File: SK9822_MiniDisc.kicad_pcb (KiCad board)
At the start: 4 copper layers, 220 x 220 mm, 342 parts, among them P1 CONN_01X04, P2 CONN_01X04

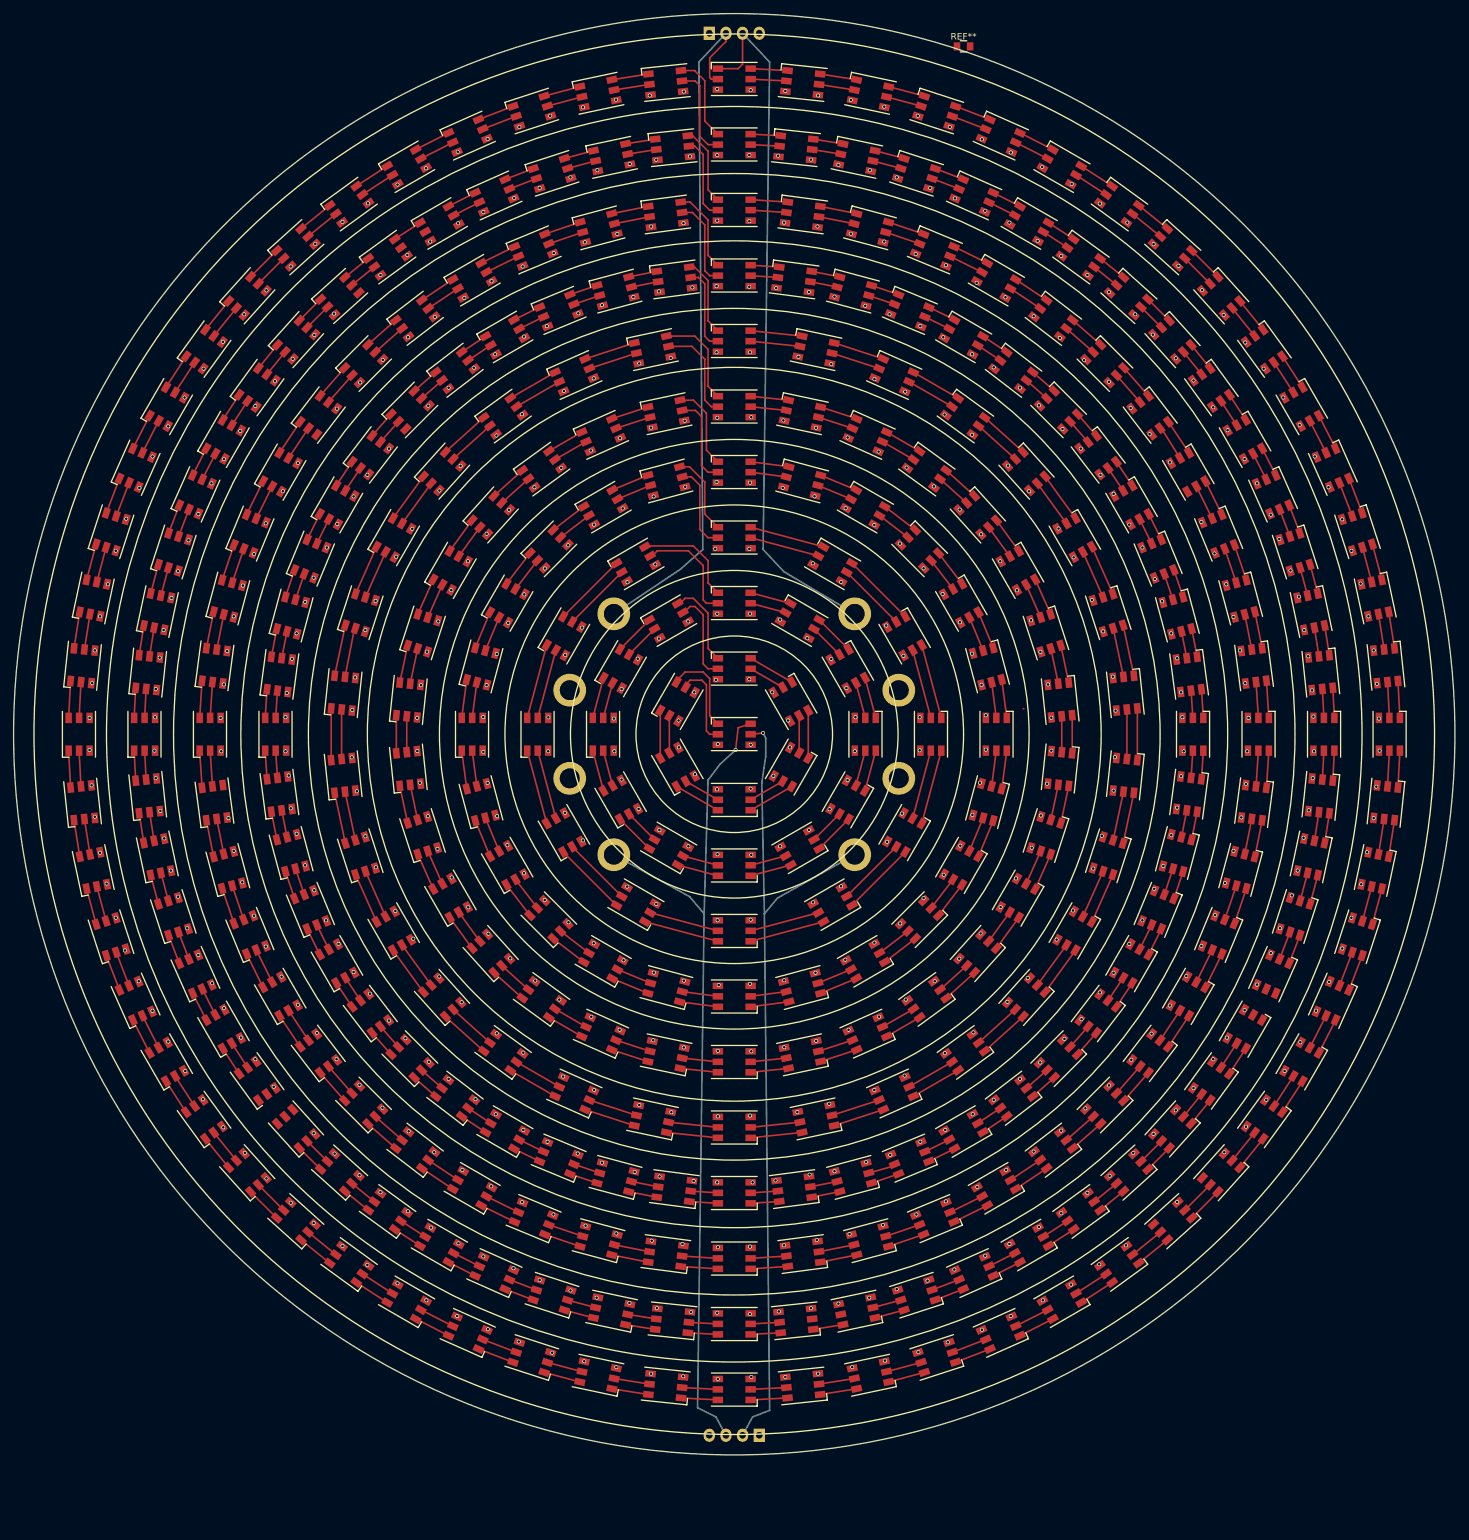
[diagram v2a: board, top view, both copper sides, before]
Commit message: places caps
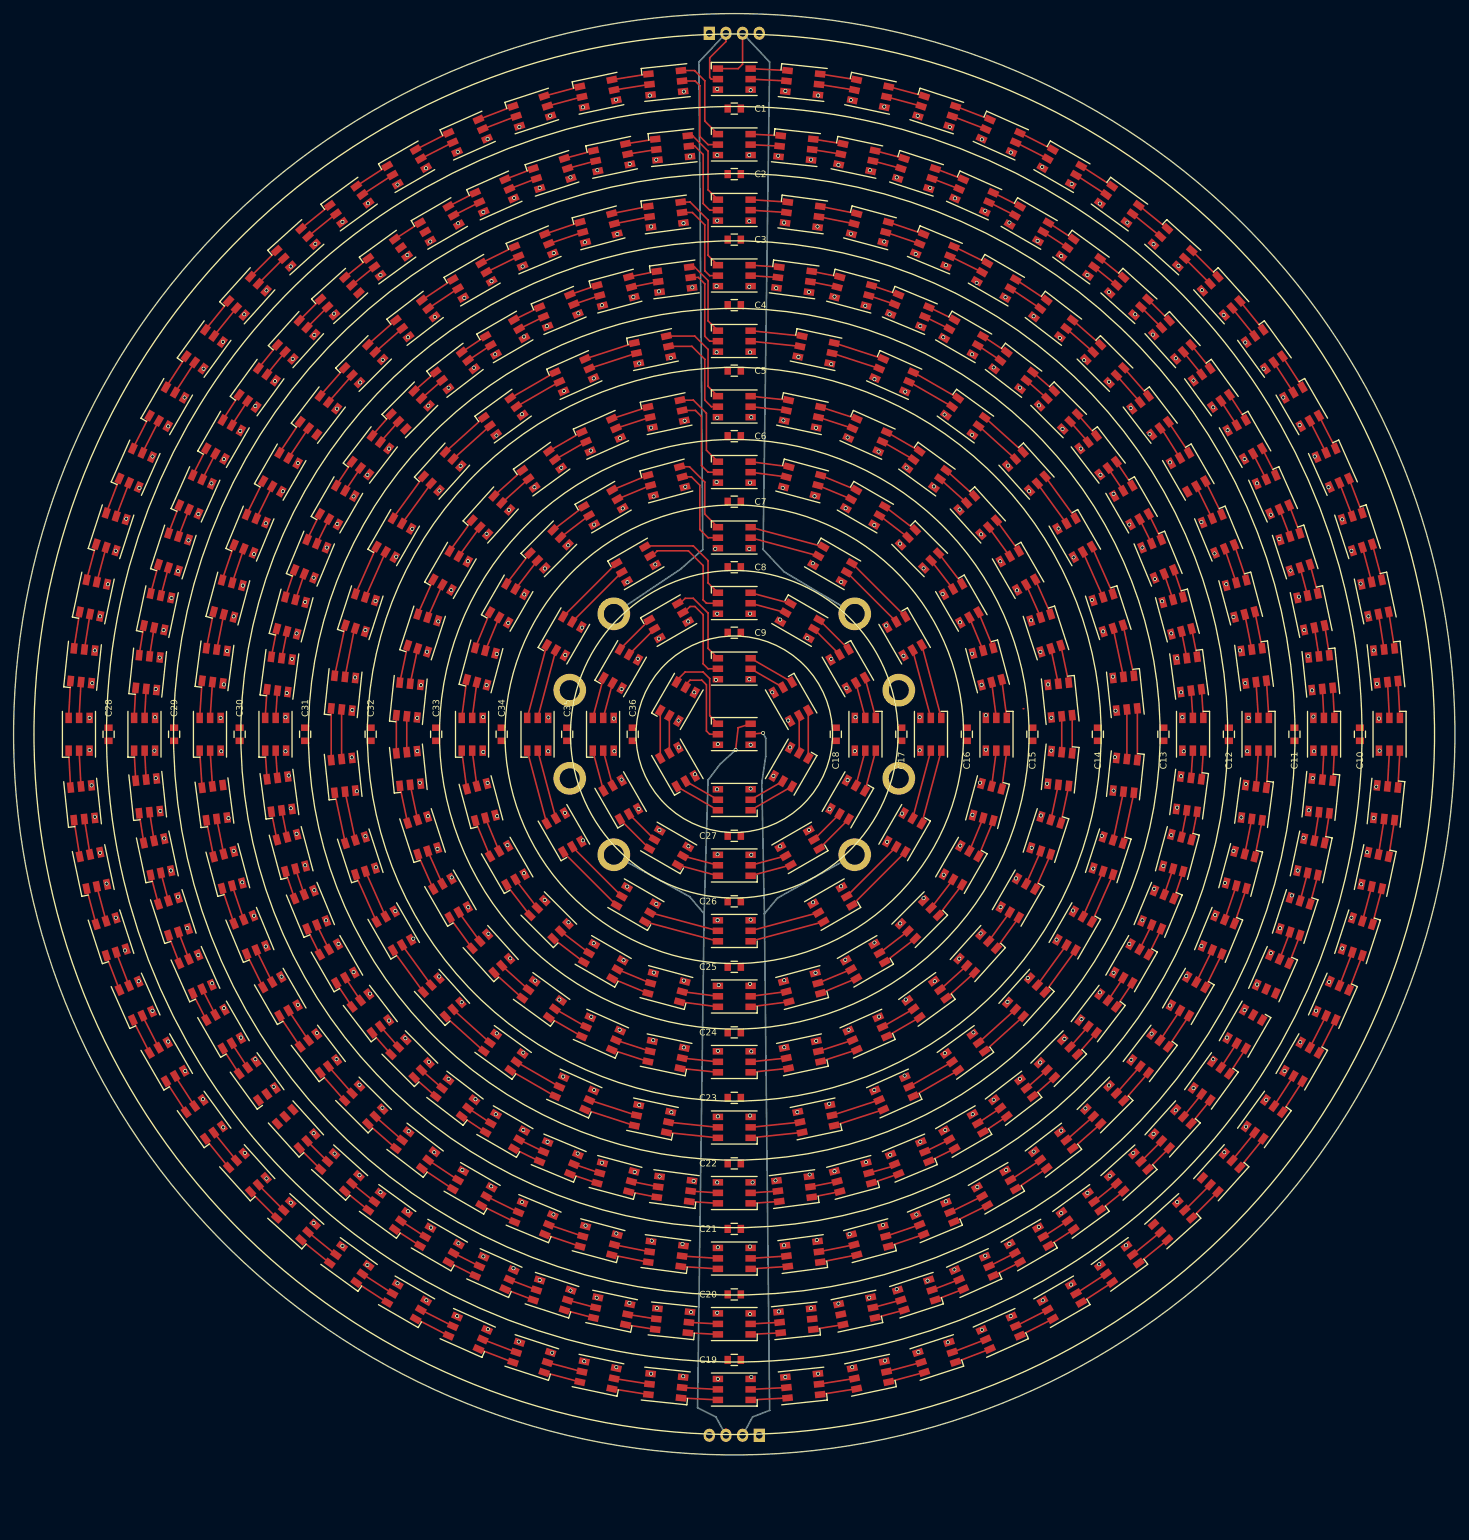
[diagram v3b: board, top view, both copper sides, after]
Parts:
- added C10: C_0805, Capacitors_SMD:C_0805, F.Cu at (395.5, 200.0)
- added C11: C_0805, Capacitors_SMD:C_0805, F.Cu at (385.5, 200.0)
- added C12: C_0805, Capacitors_SMD:C_0805, F.Cu at (375.5, 200.0)
- added C13: C_0805, Capacitors_SMD:C_0805, F.Cu at (365.5, 200.0)
- added C14: C_0805, Capacitors_SMD:C_0805, F.Cu at (355.5, 200.0)
- added C15: C_0805, Capacitors_SMD:C_0805, F.Cu at (345.5, 200.0)
- added C16: C_0805, Capacitors_SMD:C_0805, F.Cu at (335.5, 200.0)
- added C17: C_0805, Capacitors_SMD:C_0805, F.Cu at (325.5, 200.0)
- added C18: C_0805, Capacitors_SMD:C_0805, F.Cu at (315.5, 200.0)
- added C19: C_0805, Capacitors_SMD:C_0805, F.Cu at (300.0, 295.5)
- added C2: C_0805, Capacitors_SMD:C_0805, F.Cu at (300.0, 114.5)
- added C20: C_0805, Capacitors_SMD:C_0805, F.Cu at (300.0, 285.5)
- added C21: C_0805, Capacitors_SMD:C_0805, F.Cu at (300.0, 275.5)
- added C22: C_0805, Capacitors_SMD:C_0805, F.Cu at (300.0, 265.5)
- added C23: C_0805, Capacitors_SMD:C_0805, F.Cu at (300.0, 255.5)
- added C24: C_0805, Capacitors_SMD:C_0805, F.Cu at (300.0, 245.5)
- added C25: C_0805, Capacitors_SMD:C_0805, F.Cu at (300.0, 235.5)
- added C26: C_0805, Capacitors_SMD:C_0805, F.Cu at (300.0, 225.5)
- added C27: C_0805, Capacitors_SMD:C_0805, F.Cu at (300.0, 215.5)
- added C28: C_0805, Capacitors_SMD:C_0805, F.Cu at (204.5, 200.0)
- added C29: C_0805, Capacitors_SMD:C_0805, F.Cu at (214.5, 200.0)
- added C3: C_0805, Capacitors_SMD:C_0805, F.Cu at (300.0, 124.5)
- added C30: C_0805, Capacitors_SMD:C_0805, F.Cu at (224.5, 200.0)
- added C31: C_0805, Capacitors_SMD:C_0805, F.Cu at (234.5, 200.0)
- added C32: C_0805, Capacitors_SMD:C_0805, F.Cu at (244.5, 200.0)
- added C33: C_0805, Capacitors_SMD:C_0805, F.Cu at (254.5, 200.0)
- added C34: C_0805, Capacitors_SMD:C_0805, F.Cu at (264.5, 200.0)
- added C35: C_0805, Capacitors_SMD:C_0805, F.Cu at (274.5, 200.0)
- added C36: C_0805, Capacitors_SMD:C_0805, F.Cu at (284.5, 200.0)
- added C4: C_0805, Capacitors_SMD:C_0805, F.Cu at (300.0, 134.5)
- added C5: C_0805, Capacitors_SMD:C_0805, F.Cu at (300.0, 144.5)
- added C6: C_0805, Capacitors_SMD:C_0805, F.Cu at (300.0, 154.5)
- added C7: C_0805, Capacitors_SMD:C_0805, F.Cu at (300.0, 164.5)
- added C8: C_0805, Capacitors_SMD:C_0805, F.Cu at (300.0, 174.5)
- added C9: C_0805, Capacitors_SMD:C_0805, F.Cu at (300.0, 184.5)
- moved C1 36.3 mm to (300.0, 104.5)
- renumbered REF** to C1

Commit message: finaly got caps right
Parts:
- added C37, C38, C39, C40: 10uF, Capacitors_SMD:C_0805, F.Cu at (300.0, 320.1)
- C1, C10, C11, C12, C13, C14, C15, C16, C17, C18, C19, C2, C20, C21, C22, C23, C24, C25, C26, C27, C28, C29, C3, C30, C31, C32, C33, C34, C35, C36, C4, C5, C6, C7, C8, C9: value C_0805 -> 10uF
- turned C1 to 180 degrees
- turned C10 to 90 degrees
- turned C11 to 90 degrees
- turned C12 to 90 degrees
- turned C13 to 90 degrees
- turned C14 to 90 degrees
- turned C15 to 90 degrees
- turned C16 to 90 degrees
- turned C17 to 90 degrees
- turned C18 to 90 degrees
- turned C19 to 0 degrees
- turned C2 to 180 degrees
- turned C20 to 0 degrees
- turned C21 to 0 degrees
- turned C22 to 0 degrees
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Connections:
- C1 pad 1: (no net) -> VCC
- C1 pad 2: (no net) -> GND
- C10 pad 1: (no net) -> VCC
- C10 pad 2: (no net) -> GND
- C11 pad 1: (no net) -> VCC
- C11 pad 2: (no net) -> GND
- C12 pad 1: (no net) -> VCC
- C12 pad 2: (no net) -> GND
- C13 pad 1: (no net) -> VCC
- C13 pad 2: (no net) -> GND
- C14 pad 1: (no net) -> VCC
- C14 pad 2: (no net) -> GND
- C15 pad 1: (no net) -> VCC
- C15 pad 2: (no net) -> GND
- C16 pad 1: (no net) -> VCC
- C16 pad 2: (no net) -> GND
- C17 pad 1: (no net) -> VCC
- C17 pad 2: (no net) -> GND
- C18 pad 1: (no net) -> VCC
- C18 pad 2: (no net) -> GND
- C19 pad 1: (no net) -> VCC
- C19 pad 2: (no net) -> GND
- C2 pad 1: (no net) -> VCC
- C2 pad 2: (no net) -> GND
- C20 pad 1: (no net) -> VCC
- C20 pad 2: (no net) -> GND
- C21 pad 1: (no net) -> VCC
- C21 pad 2: (no net) -> GND
- C22 pad 1: (no net) -> VCC
- C22 pad 2: (no net) -> GND
- C23 pad 1: (no net) -> VCC
- C23 pad 2: (no net) -> GND
- C24 pad 1: (no net) -> VCC
- C24 pad 2: (no net) -> GND
- C25 pad 1: (no net) -> VCC
- C25 pad 2: (no net) -> GND
- C26 pad 1: (no net) -> VCC
- C26 pad 2: (no net) -> GND
- C27 pad 1: (no net) -> VCC
- C27 pad 2: (no net) -> GND
- C28 pad 1: (no net) -> VCC
- C28 pad 2: (no net) -> GND
- C29 pad 1: (no net) -> VCC
- C29 pad 2: (no net) -> GND
- C3 pad 1: (no net) -> VCC
- C3 pad 2: (no net) -> GND
- C30 pad 1: (no net) -> VCC
- C30 pad 2: (no net) -> GND
- C31 pad 1: (no net) -> VCC
- C31 pad 2: (no net) -> GND
- C32 pad 1: (no net) -> VCC
- C32 pad 2: (no net) -> GND
- C33 pad 1: (no net) -> VCC
- C33 pad 2: (no net) -> GND
- C34 pad 1: (no net) -> VCC
- C34 pad 2: (no net) -> GND
- C35 pad 1: (no net) -> VCC
- C35 pad 2: (no net) -> GND
- C36 pad 1: (no net) -> VCC
- C36 pad 2: (no net) -> GND
- C4 pad 1: (no net) -> VCC
- C4 pad 2: (no net) -> GND
- C5 pad 1: (no net) -> VCC
- C5 pad 2: (no net) -> GND
- C6 pad 1: (no net) -> VCC
- C6 pad 2: (no net) -> GND
- C7 pad 1: (no net) -> VCC
- C7 pad 2: (no net) -> GND
- C8 pad 1: (no net) -> VCC
- C8 pad 2: (no net) -> GND
- C9 pad 1: (no net) -> VCC
- C9 pad 2: (no net) -> GND
